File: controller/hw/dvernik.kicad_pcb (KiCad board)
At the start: 2 copper layers, 100 x 100 mm, 90 parts, among them P101 WAGO233, P102 CONN_01X06, P103 CONN_01X02, P201 WAGO255, P202 WAGO255, P401 WAGO255, P402 Wago_233-502, P403 Wago_233-502, Q201 2N7002K, Q401 IRFU9024, Q402 IRLML6402, U101 A25L40P, U102 EK-TM4C123GXL, U103 Itead_HC-05, U104 LP2992AIM5-3.3CT-ND, U201 JQX-14FC22CS8-5.0, U202 Cosmo_1010-817, U401 Mini-360, U402 Mini-360, U403 ROE-0505S, U404 HCPL-0601-500E, U405 HCPL-0601-500E, U406 Cosmo_1010-817, U407 SN75176BDR

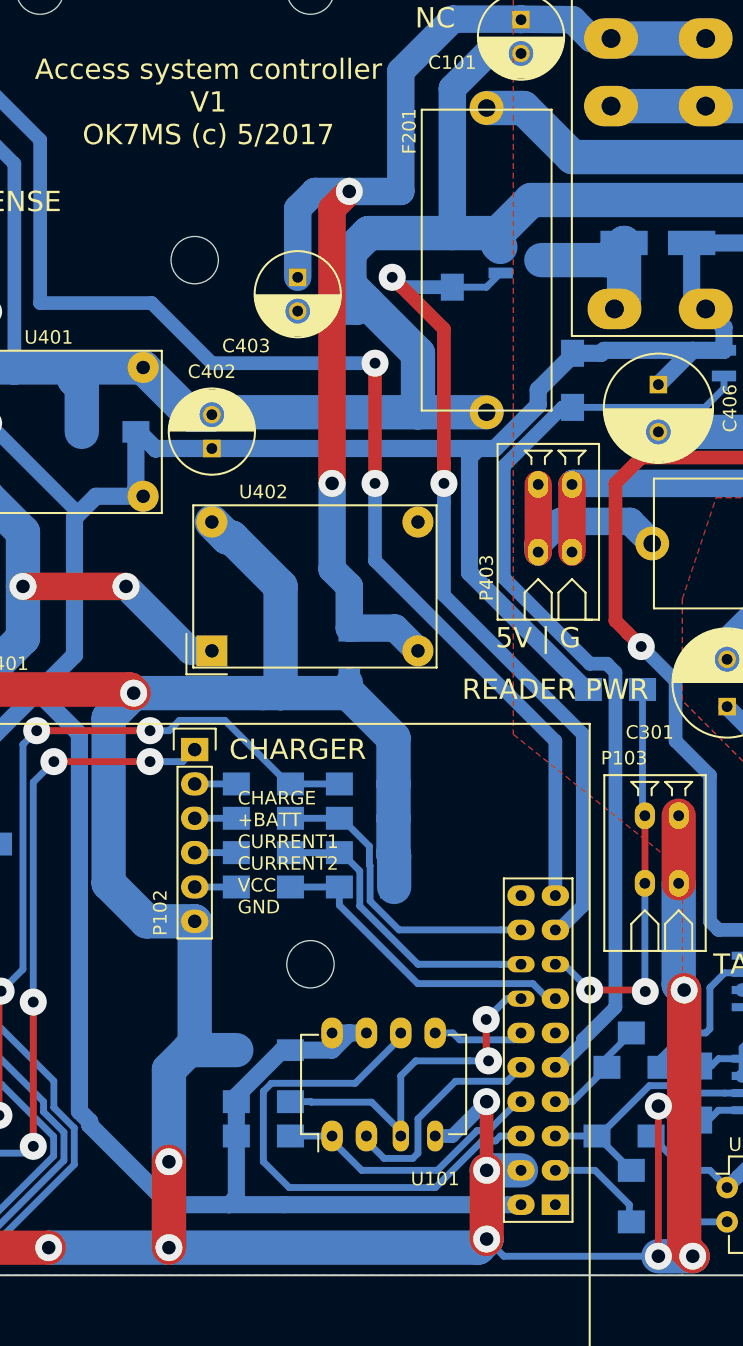
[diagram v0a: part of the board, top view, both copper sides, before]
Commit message: Fix voltage for SPI flash, short under one capacitor
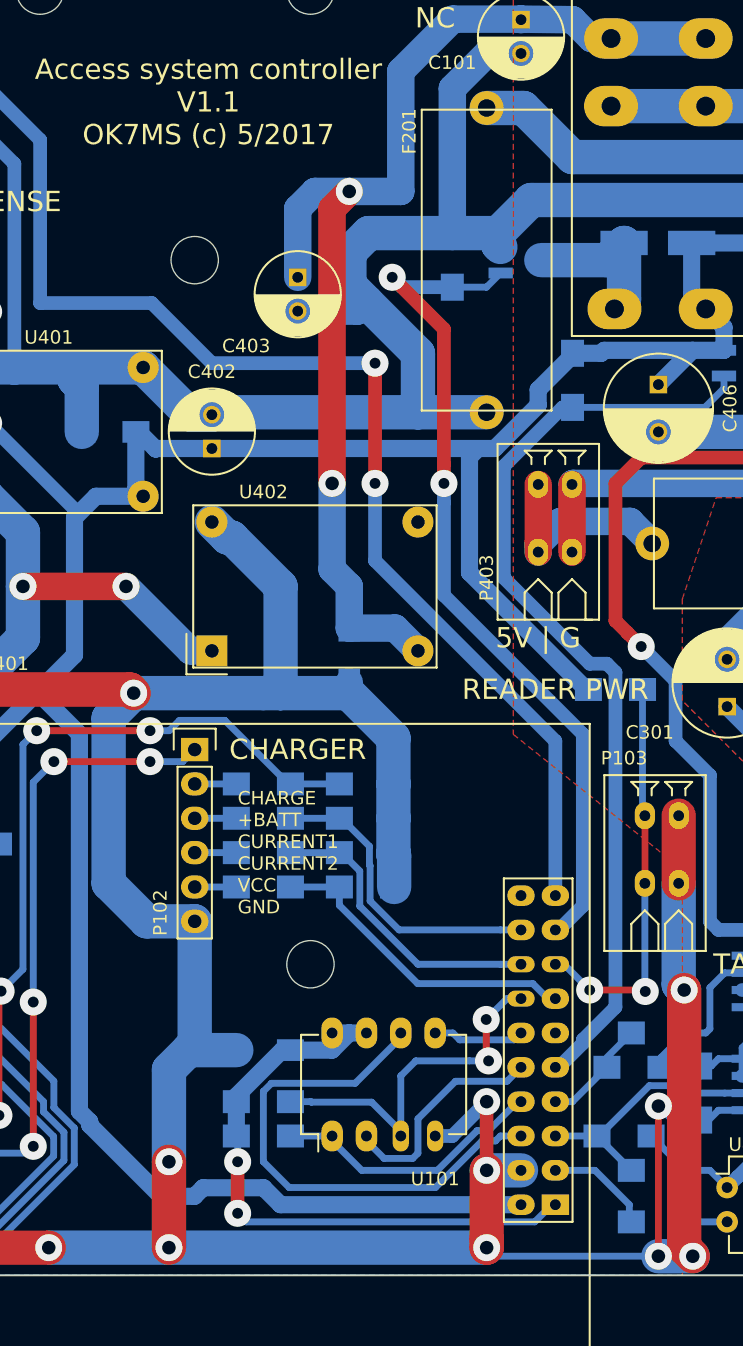
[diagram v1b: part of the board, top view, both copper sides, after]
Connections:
- C102 pad 1: +5V -> +3V3
- R101 pad 1: +5V -> +3V3
- R114 pad 1: +5V -> +3V3
- U101 pad 7: +5V -> +3V3
- U101 pad 8: +5V -> +3V3
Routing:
- net +3V3: track 0.00 -> 45.8 mm, vias 0 -> 2
- net +5V: track 281.3 -> 260.7 mm
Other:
- board text added: "Access system controller V1.1 OK7MS (c) 5/2017"
- board text removed: "Access system controller V1 OK7MS (c) 5/2017"

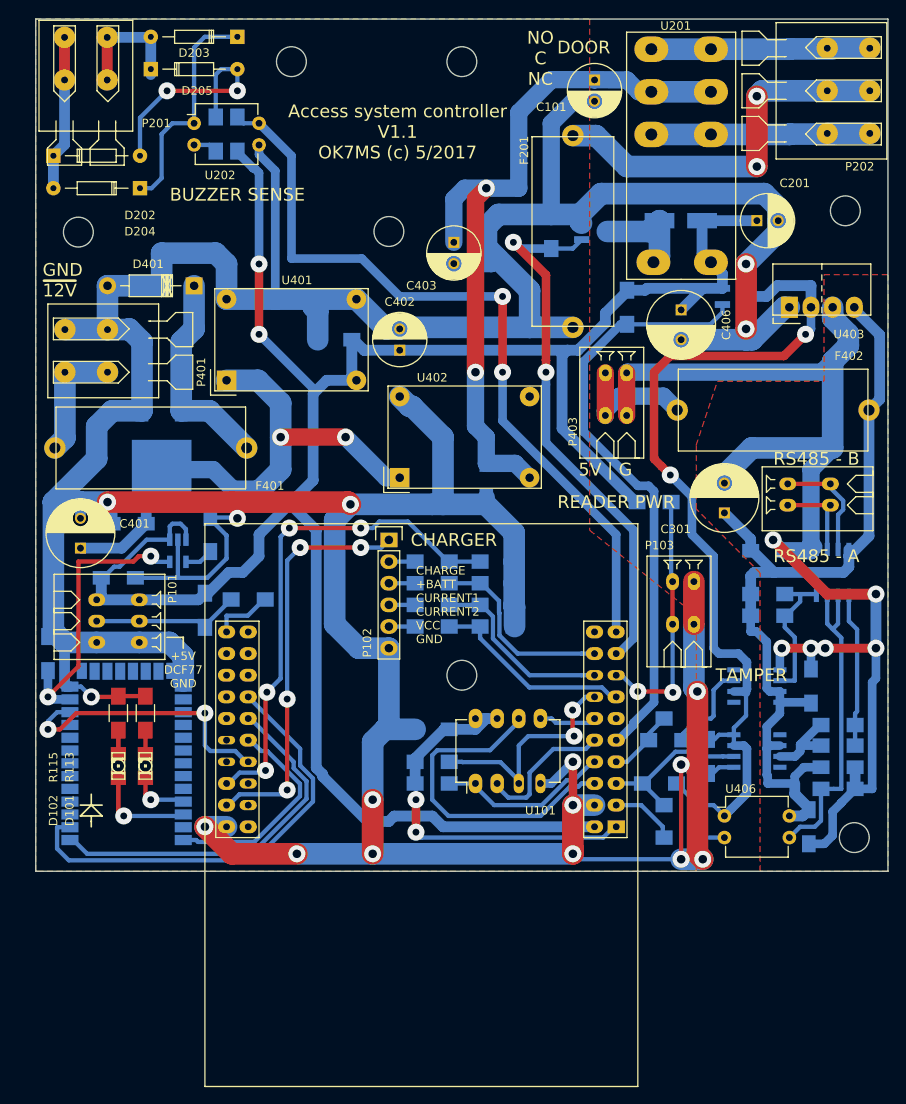
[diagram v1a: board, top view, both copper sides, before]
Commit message: Fix serious hw bug (5V level on 3.3V tolerant RX/TX on ctrl board)
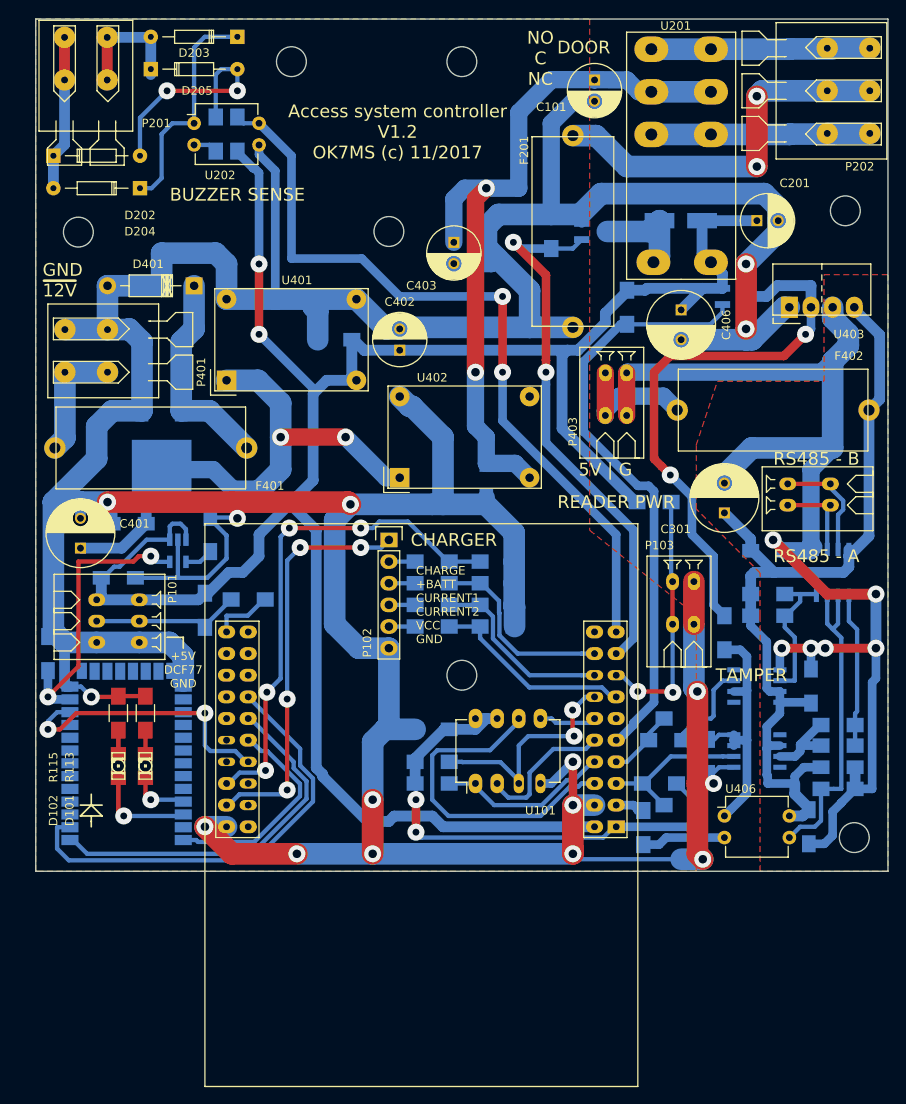
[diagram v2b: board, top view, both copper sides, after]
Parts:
- added D301: 1N4148, smd-handsolder:Diode_1206_HandSoldering, B.Cu at (130.8, 122.0)
- moved R403 4.60 mm to (121.3, 144.9), turned to 90 degrees
- turned C407 to 90 degrees
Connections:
- C407 pad 1: /ReaderIntf/DCDCIN5V -> GND
- C407 pad 2: GND -> /ReaderIntf/DC4.5V
- R402 pad 2: /ReaderIntf/DCDCIN5V -> +3V3
- R408 pad 2: /ReaderIntf/DCDCIN5V -> +3V3
- U404 pad 7: /ReaderIntf/DCDCIN5V -> /ReaderIntf/DC4.5V
- U404 pad 8: /ReaderIntf/DCDCIN5V -> /ReaderIntf/DC4.5V
- U405 pad 2: /ReaderIntf/DCDCIN5V -> /ReaderIntf/DC4.5V
- U406 pad 1: /ReaderIntf/DCDCIN5V -> /ReaderIntf/DC4.5V
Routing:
- net /ReaderIntf/DCDCIN5V: track 106.3 -> 65.5 mm
- net /ReaderIntf/DC4.5V: track 0.00 -> 30.4 mm
- net +3V3: track 45.8 -> 61.3 mm
- net GND: track 583.0 -> 571.7 mm, vias 17 -> 16
- net Net-(R403-Pad1): track 3.08 -> 9.87 mm
- net /~TX_EN: track 7.85 -> 4.41 mm
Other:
- board text added: "Access system controller V1.2 OK7MS (c) 11/2017"
- board text removed: "Access system controller V1.1 OK7MS (c) 5/2017"

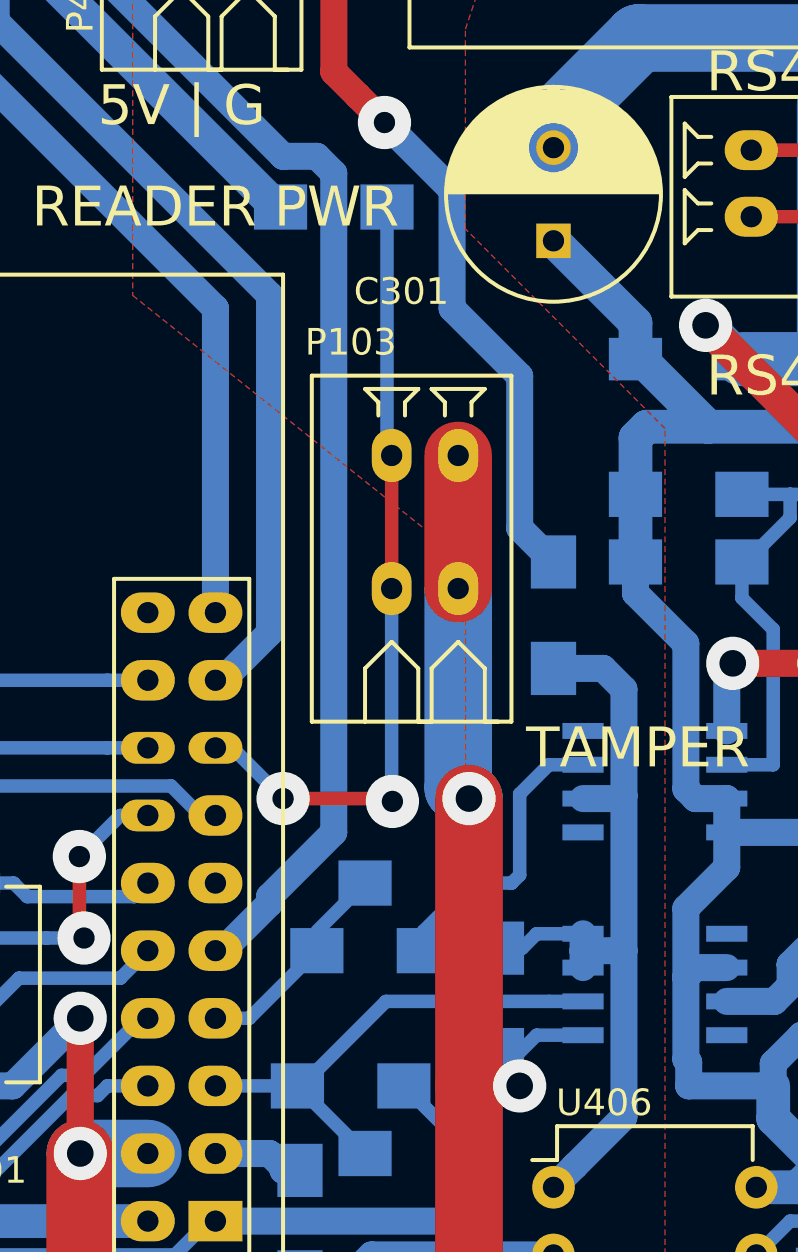
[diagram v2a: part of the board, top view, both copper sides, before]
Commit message: Fix controller issues with 3.3V CPU interfacing 5V logic
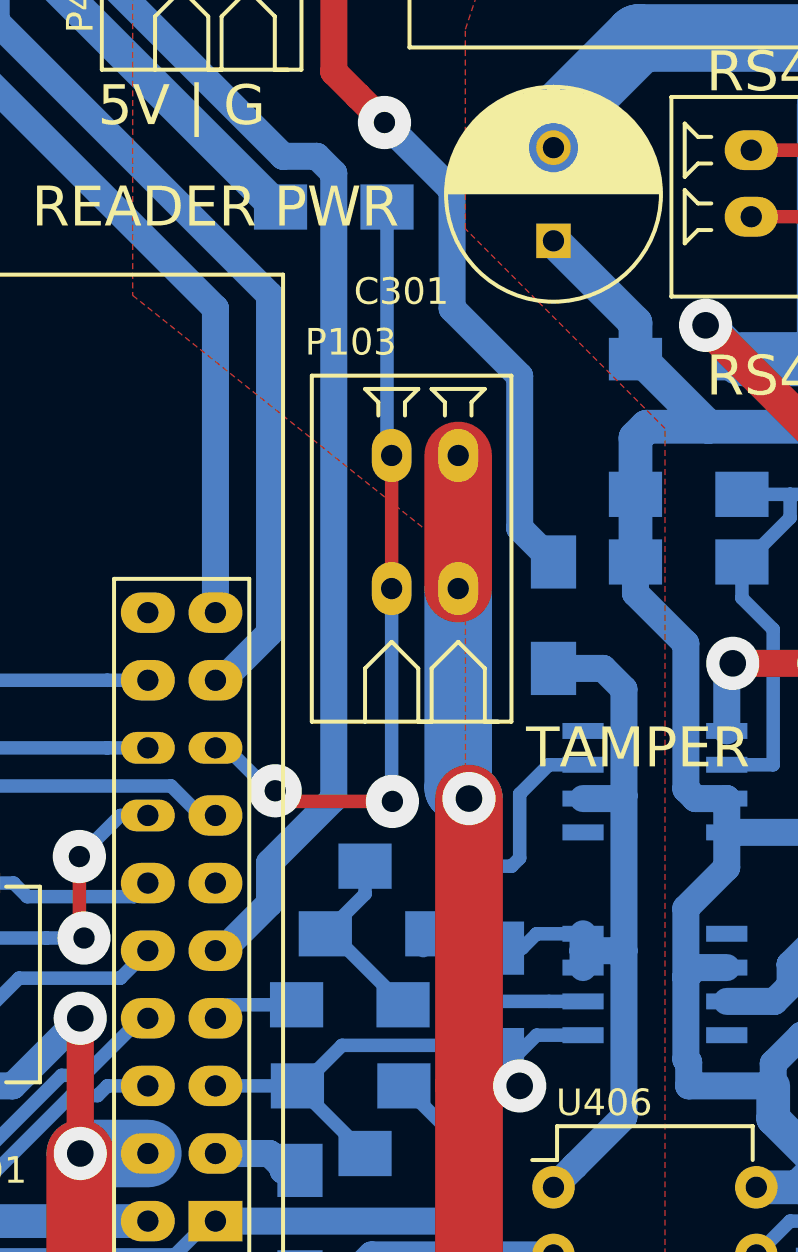
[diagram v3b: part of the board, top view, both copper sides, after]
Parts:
- added D302: TS4148RXG, smd-handsolder:Diode_1206_HandSoldering, B.Cu at (123.2, 136.7)
- D301: value 1N4148 -> BAT43
- moved R404 0.71 mm to (124.2, 134.0)
- moved R409 0.64 mm to (125.7, 131.4)
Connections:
- R404 pad 2: /CPU_TX -> /ReaderIntf/CPU_TX5
- R409 pad 2: /CPU_TX -> /ReaderIntf/CPU_TX5
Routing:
- net /ReaderIntf/CPU_TX5: track 0.00 -> 7.75 mm
- net /CPU_TX: track 7.42 -> 3.26 mm

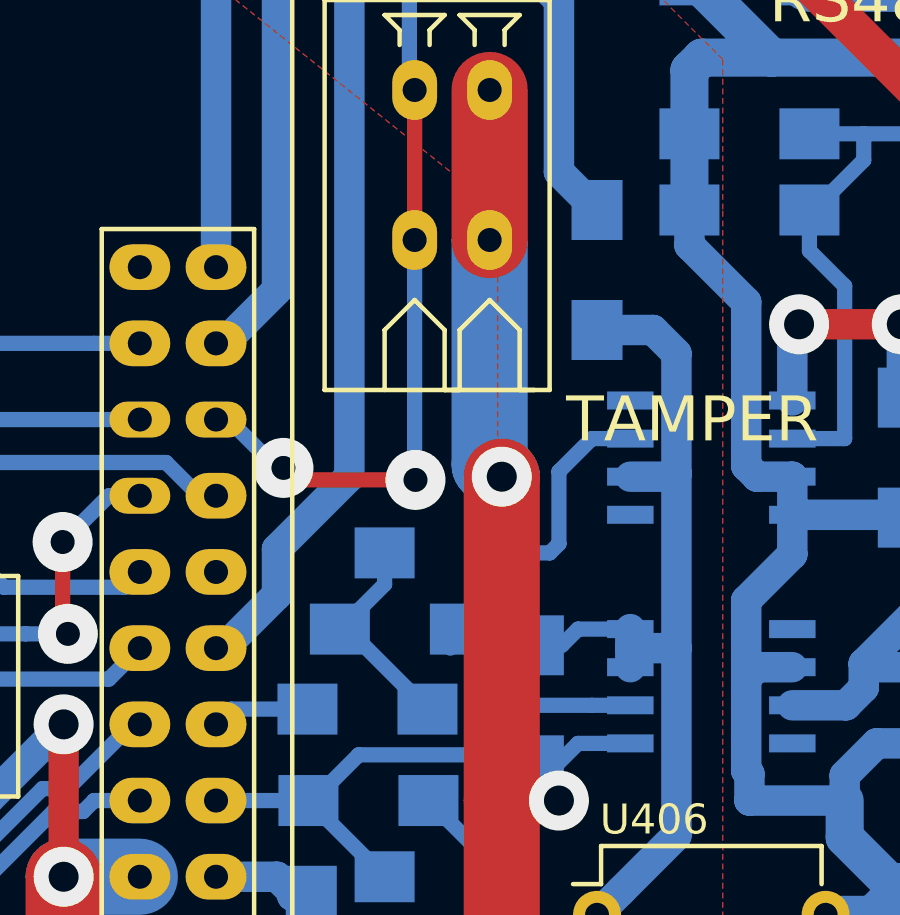
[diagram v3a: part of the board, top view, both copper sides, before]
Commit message: WIP Still working in 3.3 - 5V interface issues
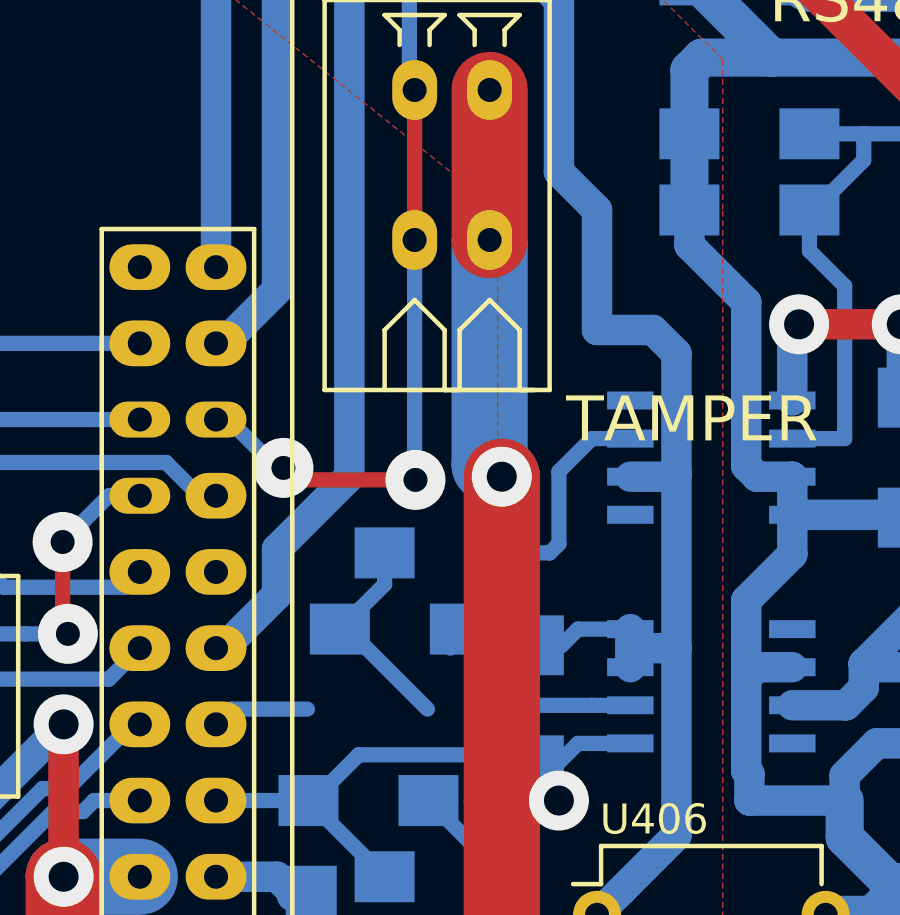
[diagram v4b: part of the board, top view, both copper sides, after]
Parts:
- removed D301: BAT43, smd-handsolder:Diode_1206_HandSoldering
- removed D302: TS4148RXG, smd-handsolder:Diode_1206_HandSoldering
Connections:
- C407 pad 2: /ReaderIntf/DC4.5V -> /ReaderIntf/DCDCIN5V
- Q402 pad 1: /~READER_ON -> /ReaderIntf/~READER_ON
- R401 pad 1: /~READER_ON -> /ReaderIntf/~READER_ON
- U404 pad 7: /ReaderIntf/DC4.5V -> /ReaderIntf/DCDCIN5V
- U404 pad 8: /ReaderIntf/DC4.5V -> /ReaderIntf/DCDCIN5V
- U405 pad 2: /ReaderIntf/DC4.5V -> /ReaderIntf/DCDCIN5V
- U406 pad 1: /ReaderIntf/DC4.5V -> /ReaderIntf/DCDCIN5V
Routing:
- net /~READER_ON: track 70.2 -> 0.00 mm
- net /ReaderIntf/~READER_ON: track 0.00 -> 70.2 mm
- net /ReaderIntf/DCDCIN5V: track 65.5 -> 99.9 mm
- net /ReaderIntf/DC4.5V: track 30.4 -> 0.00 mm
